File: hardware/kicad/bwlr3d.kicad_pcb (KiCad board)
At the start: 2 copper layers, 36.8 x 90.9 mm, 107 parts, among them Q1 AO3407, Q2 DMG1012UW, Q3 PMV32UP, Q4 DMG1012UW, SW3 RESET, SW4 BOOT, U1 BME680, U2 RAK3172, U3 AEM10941-QFN, U4 XC6215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

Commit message: update library and footprint
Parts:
- C14, C23: value 1uf -> 1uF
- R12, R13: value 65 -> 1K

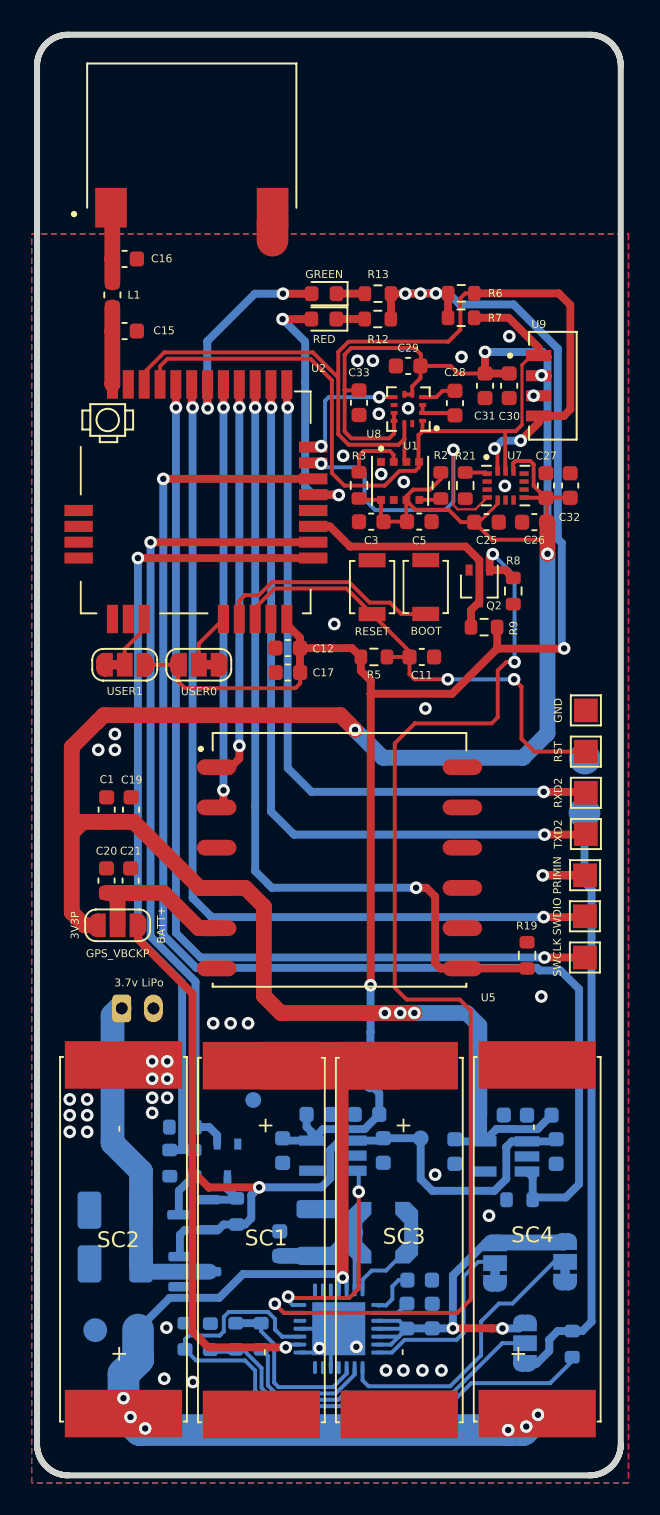
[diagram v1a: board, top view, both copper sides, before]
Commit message: switch IMU_INT with BATT_MEAS, switch I2C pull-up to 3V3P, and add GND stitch
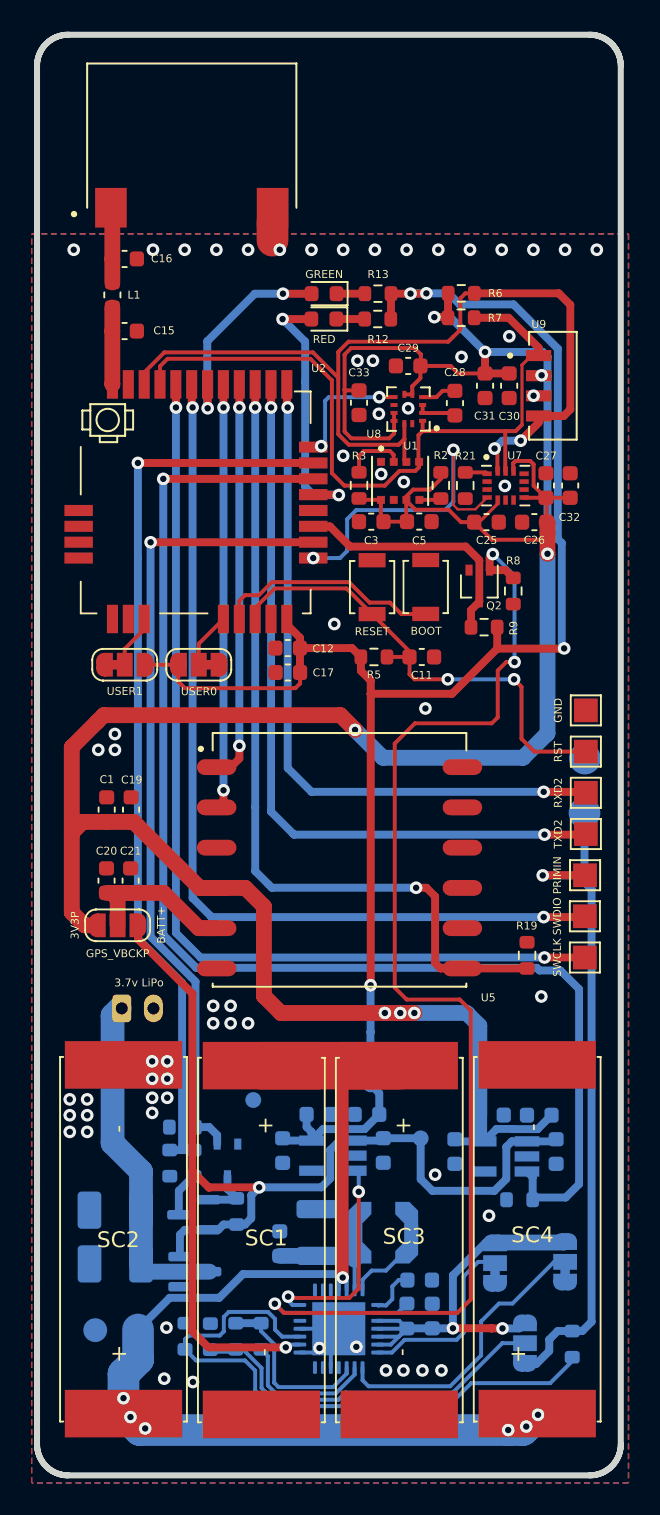
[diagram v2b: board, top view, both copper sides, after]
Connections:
- R6 pad 1: +3.3V -> +3.3VP
- R7 pad 1: +3.3V -> +3.3VP
- U2 pad 25: /BATT_MEAS -> /IMU_INT
- U2 pad 31: /IMU_INT -> /BATT_MEAS
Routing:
- net /BATT_MEAS: track 51.2 -> 57.7 mm
- net +3.3VP: track 182.1 -> 188.6 mm, vias 7 -> 8
- net +3.3V: track 109.2 -> 105.7 mm, vias 5 -> 4
- net Net-(C34-Pad1): track 9.00 -> 8.45 mm
- net GND: vias 44 -> 62

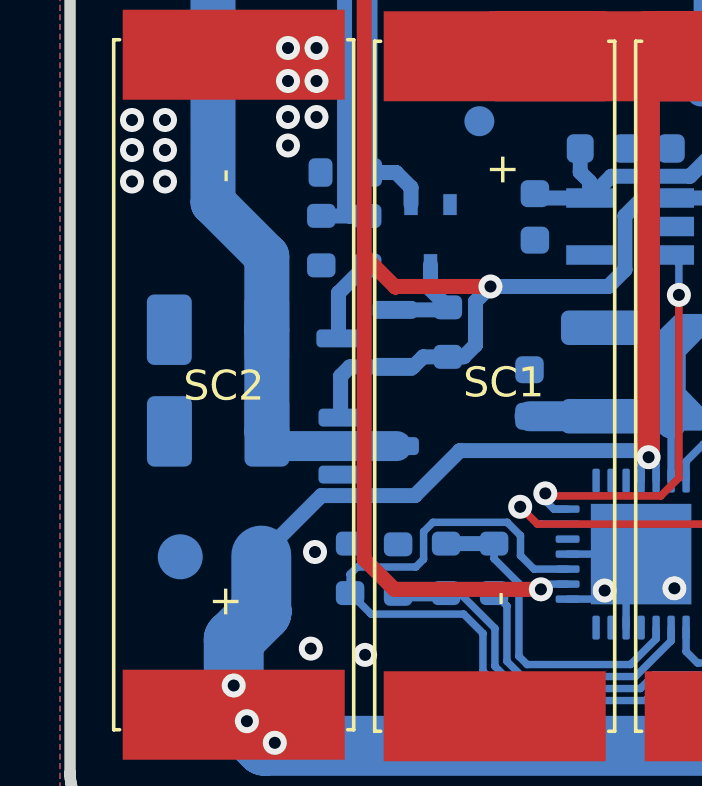
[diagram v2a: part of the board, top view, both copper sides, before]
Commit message: change voltage divider value to 4.7K and 10K, add 0.1uF capacitor to voltage divider
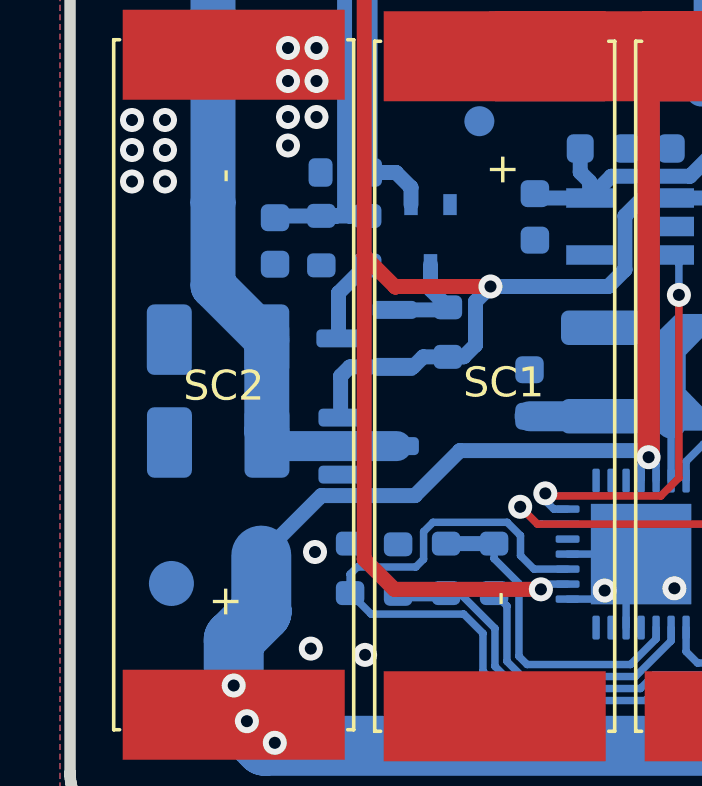
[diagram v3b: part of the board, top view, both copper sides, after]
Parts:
- added C35: 0.1uF, Capacitor_SMD:C_0603_1608Metric, B.Cu at (134.5, 126.6)
- R1: value 4.7M -> 4.7K
- R4: value 10M -> 10K
- moved TP11 0.94 mm to (131.1, 138.0)
- moved C4 0.37 mm to (132.6, 133.3)
- moved C2 0.33 mm to (132.6, 129.9)
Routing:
- net /BATT_MEAS: track 57.7 -> 59.8 mm
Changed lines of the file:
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@@
   )
   (footprint "Capacitor_Tantalum_SMD:CP_EIA-3528-15_AVX-H_Pad1.50x2.35mm_HandSolder" (layer "B.Cu")
-    (at 132.61875 129.59 180)
+    (at 132.61875 129.921 180)
     (descr "Tantalum Capacitor SMD AVX-H (3528-15 Metric), IPC_7351 nominal, (Body size from: http://www.kemet.com/Lists/ProductCatalog/Attachments/253/KEM_TC101_STD.pdf), generated with kicad-footprint-generator")
     (tags "capacitor tantalum")
@@
   )
   (footprint "Capacitor_Tantalum_SMD:CP_EIA-3528-15_AVX-H_Pad1.50x2.35mm_HandSolder" (layer "B.Cu")
-    (at 132.62375 132.98 180)
+    (at 132.62375 133.35 180)
     (descr "Tantalum Capacitor SMD AVX-H (3528-15 Metric), IPC_7351 nominal, (Body size from: http://www.kemet.com/Lists/ProductCatalog/Attachments/253/KEM_TC101_STD.pdf), generated with kicad-footprint-generator")
     (tags "capacitor tantalum")
@@
     (property "Sheetname" "")
     (attr smd)
-    (fp_text reference "R4" (at 0.01 1.07125 90) (layer "B.SilkS")
+    (fp_text reference "R4" (at -2.033 1.057 90) (layer "B.SilkS")
       (effects (font (size 0.5 0.5) (thickness 0.125)) (justify mirror))
     )
-    (fp_text value "10M" (at -1.23 1.08 90) (layer "B.Fab")
+    (fp_text value "10K" (at -1.23 1.08 90) (layer "B.Fab")
       (effects (font (size 0.5 0.5) (thickness 0.125)) (justify mirror))
     )
@@
   )
   (footprint "TestPoint:TestPoint_Pad_D1.5mm" (layer "B.Cu")
-    (at 131.35875 137.16 -90)
+    (at 131.064 138.049 -90)
     (descr "SMD pad as test Point, diameter 1.5mm")
     (tags "test point SMD pad")
@@
       (effects (font (size 0.5 0.5) (thickness 0.125)) (justify mirror))
     )
-    (fp_text value "4.7M" (at 0.005 0 90) (layer "B.Fab")
+    (fp_text value "4.7K" (at 0.005 0 90) (layer "B.Fab")
       (effects (font (size 0.5 0.5) (thickness 0.125)) (justify mirror))
     )
@@
     )
   )
+  (footprint "Capacitor_SMD:C_0603_1608Metric" (layer "B.Cu")
+    (at 134.5184 126.632 90)
+    (descr "Capacitor SMD 0603 (1608 Metric), square (rectangular) end terminal, IPC_7351 nominal, (Body size source: IPC-SM-782 page 76, https://www.pcb-3d.com/wordpress/wp-content/uploads/ipc-sm-782a_amendment_1_and_2.pdf), generated with kicad-footprint-generator")
+    (tags "capacitor")
+    (property "Sheetfile" "bwlr3d.kicad_sch")
+    (property "Sheetname" "")
+    (attr smd)
+    (fp_text reference "C35" (at -0.635 -1.27 270) (layer "B.SilkS")
+      (effects (font (size 0.5 0.5) (thickness 0.125)) (justify mirror))
+    )
+    (fp_text value "0.1uF" (at 0 -1.43 90) (layer "B.Fab")
+      (effects (font (size 1 1) (thickness 0.15)) (justify mirror))
+    )
+    (fp_text user "${REFERENCE}" (at 0 0 90) (layer "B.Fab")
+      (effects (font (size 0.4 0.4) (thickness 0.06)) (justify mirror))
+    )
+    (fp_line (start -0.14058 0.51) (end 0.14058 0.51) (layer "B.SilkS") (width 0.12))
+    (fp_line (start -0.14058 -0.51) (end 0.14058 -0.51) (layer "B.SilkS") (width 0.12))
+    (fp_line (start -1.48 -0.73) (end -1.48 0.73) (layer "B.CrtYd") (width 0.05))
+    (fp_line (start 1.48 0.73) (end 1.48 -0.73) (layer "B.CrtYd") (width 0.05))
+    (fp_line (start 1.48 -0.73) (end -1.48 -0.73) (layer "B.CrtYd") (width 0.05))
+    (fp_line (start -1.48 0.73) (end 1.48 0.73) (layer "B.CrtYd") (width 0.05))
+    (fp_line (start -0.8 0.4) (end 0.8 0.4) (layer "B.Fab") (width 0.1))
+    (fp_line (start 0.8 -0.4) (end -0.8 -0.4) (layer "B.Fab") (width 0.1))
+    (fp_line (start -0.8 -0.4) (end -0.8 0.4) (layer "B.Fab") (width 0.1))
+    (fp_line (start 0.8 0.4) (end 0.8 -0.4) (layer "B.Fab") (width 0.1))
+    (pad "1" smd roundrect (at -0.775 0 90) (size 0.9 0.95) (layers "B.Cu" "B.Paste" "B.Mask") (roundrect_rratio 0.25)
+      (net 2 "GND") (pintype "passive"))
+    (pad "2" smd roundrect (at 0.775 0 90) (size 0.9 0.95) (layers "B.Cu" "B.Paste" "B.Mask") (roundrect_rratio 0.25)
+      (net 17 "/BATT_MEAS") (pintype "passive"))
+    (model "${KICAD6_3DMODEL_DIR}/Capacitor_SMD.3dshapes/C_0603_1608Metric.wrl"
+      (offset (xyz 0 0 0))
+      (scale (xyz 1 1 1))
+      (rotate (xyz 0 0 0))
+    )
+  )
   (footprint "Resistor_SMD:R_0603_1608Metric" (layer "B.Cu")
     (at 137.02 137.545 90)
@@
   (segment (start 137.89 95.18) (end 137.89 93.8575) (width 0.25) (layer "F.Cu") (net 3))
   (segment (start 137.89 93.8575) (end 139.4475 92.3) (width 0.25) (layer "F.Cu") (net 3))
+  (segment (start 132.45 125.35) (end 132.45 128.12725) (width 1.5) (layer "B.Cu") (net 4))
   (segment (start 134.73875 133.47) (end 134.24875 132.98) (width 1) (layer "B.Cu") (net 4))
   (segment (start 132.45 117.3084) (end 132.8984 116.86) (width 1.5) (layer "B.Cu") (net 4))
-  (segment (start 134.24375 129.59) (end 134.24375 127.14375) (width 1.5) (layer "B.Cu") (net 4))
-  (segment (start 134.24375 127.14375) (end 132.45 125.35) (width 1.5) (layer "B.Cu") (net 4))
+  (segment (start 132.45 128.12725) (end 134.24375 129.921) (width 1.5) (layer "B.Cu") (net 4))
   (segment (start 132.45 125.35) (end 132.45 117.3084) (width 1.5) (layer "B.Cu") (net 4))
   (segment (start 134.24375 132.975) (end 134.24875 132.98) (width 1.5) (layer "B.Cu") (net 4))
@@
   (segment (start 136.065 125.8) (end 136.06 125.795) (width 0.5) (layer "B.Cu") (net 17))
   (segment (start 137.59 125.8) (end 137 125.8) (width 0.5) (layer "B.Cu") (net 17))
-  (segment (start 137 125.8) (end 136.065 125.8) (width 0.5) (layer "B.Cu") (net 17))
+  (segment (start 137 125.8) (end 136.5696 125.8) (width 0.5) (layer "B.Cu") (net 17))
+  (segment (start 134.5754 125.8) (end 134.5184 125.857) (width 0.5) (layer "B.Cu") (net 17))
   (segment (start 136.835 125.635) (end 137 125.8) (width 0.5) (layer "B.Cu") (net 17))
+  (segment (start 136.5696 125.8) (end 136.065 125.8) (width 0.5) (layer "B.Cu") (net 17))
   (segment (start 134.0515 88.45) (end 134.0515 82.4515) (width 0.5) (layer "B.Cu") (net 17))
   (segment (start 136.835 115.242714) (end 136.835 125.635) (width 0.5) (layer "B.Cu") (net 17))
@@
   (segment (start 134.0515 112.459214) (end 136.835 115.242714) (width 0.5) (layer "B.Cu") (net 17))
   (segment (start 134.0515 88.45) (end 134.0515 112.459214) (width 0.5) (layer "B.Cu") (net 17))
+  (segment (start 136.5696 125.8) (end 134.5754 125.8) (width 0.5) (layer "B.Cu") (net 17))
   (segment (start 159.785 84.645) (end 159.79 84.65) (width 0.25) (layer "F.Cu") (net 18))
   (segment (start 129.88 105.79) (end 129.88 100.38) (width 1) (layer "F.Cu") (net 18))
